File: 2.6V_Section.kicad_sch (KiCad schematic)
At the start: 1 part, among them U3_6 TPS259620DDAR

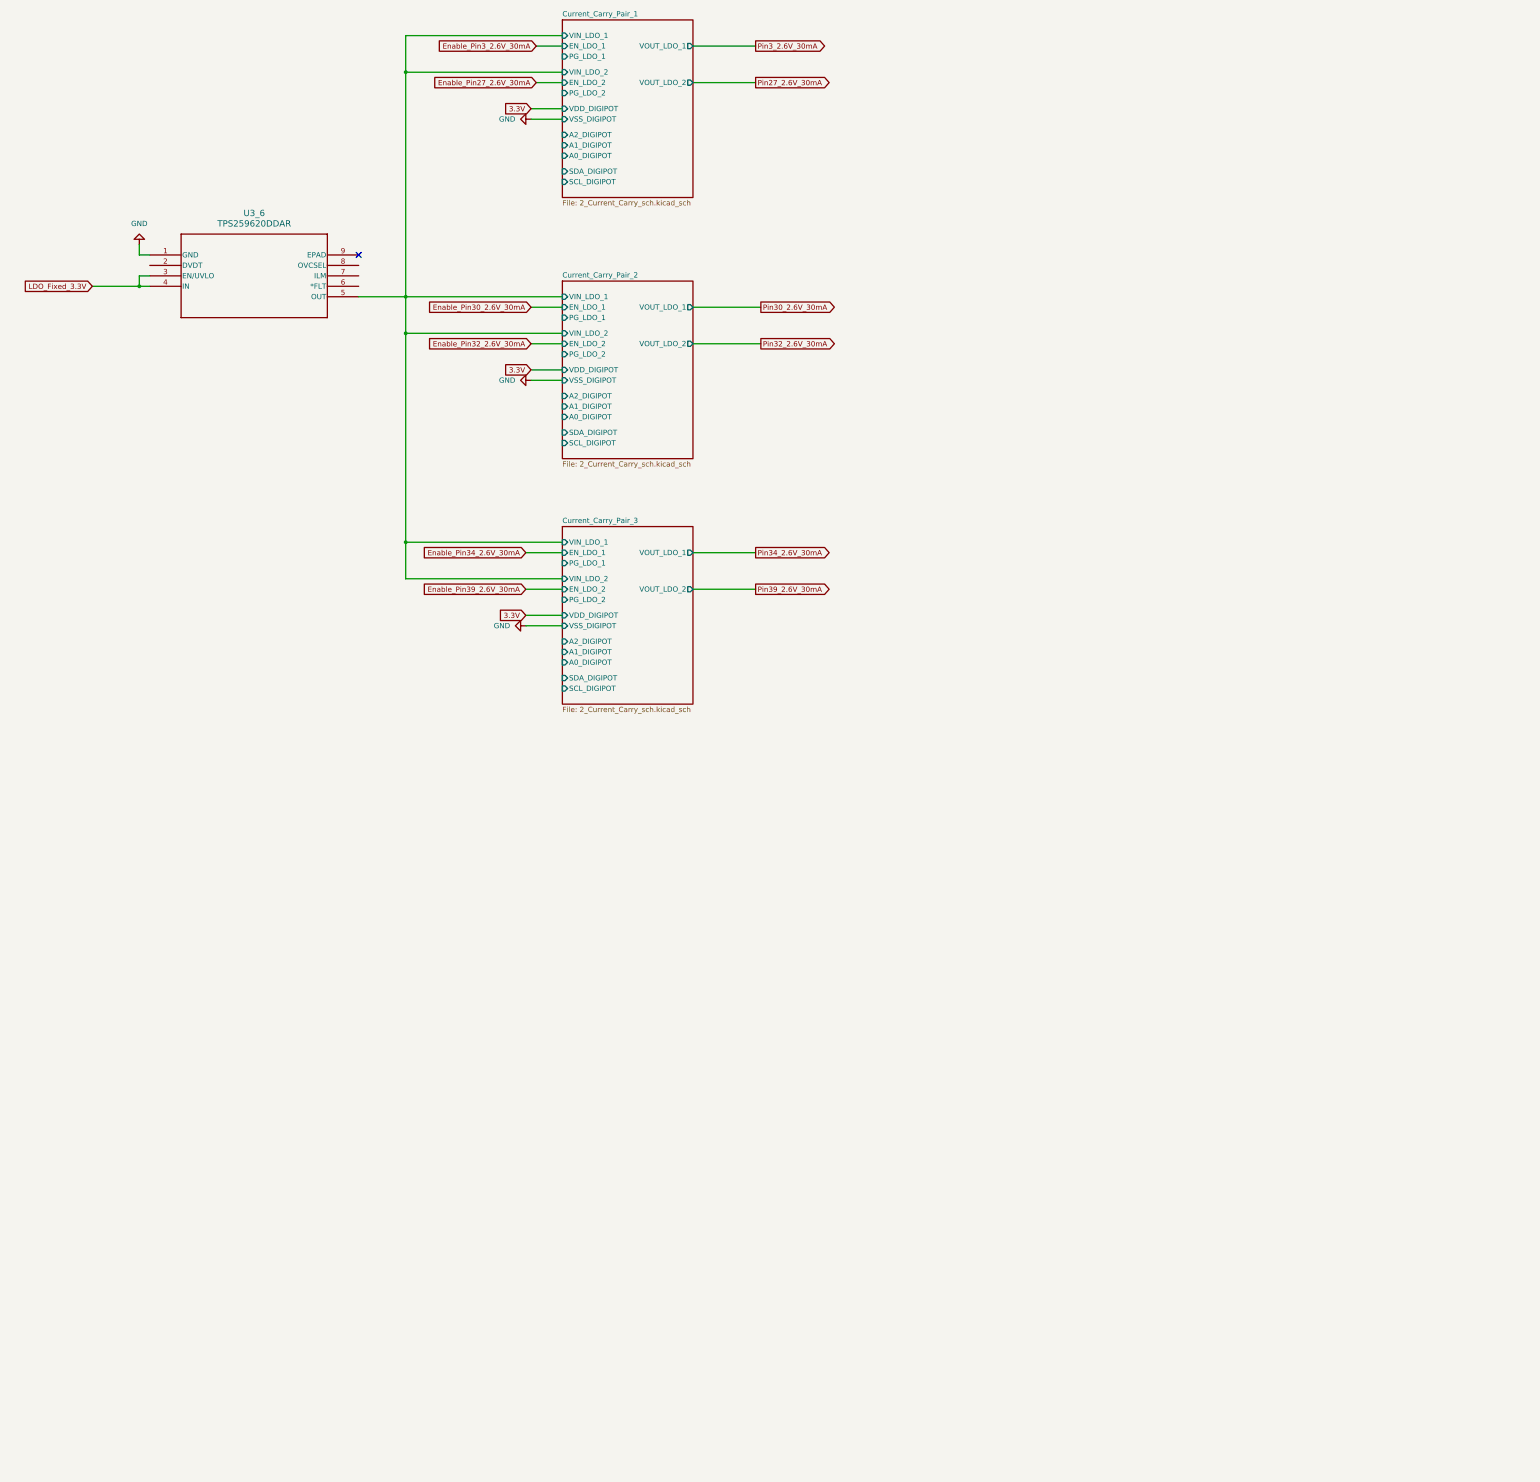
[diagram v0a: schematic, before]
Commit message: Full schematic connection without ratio consideration.
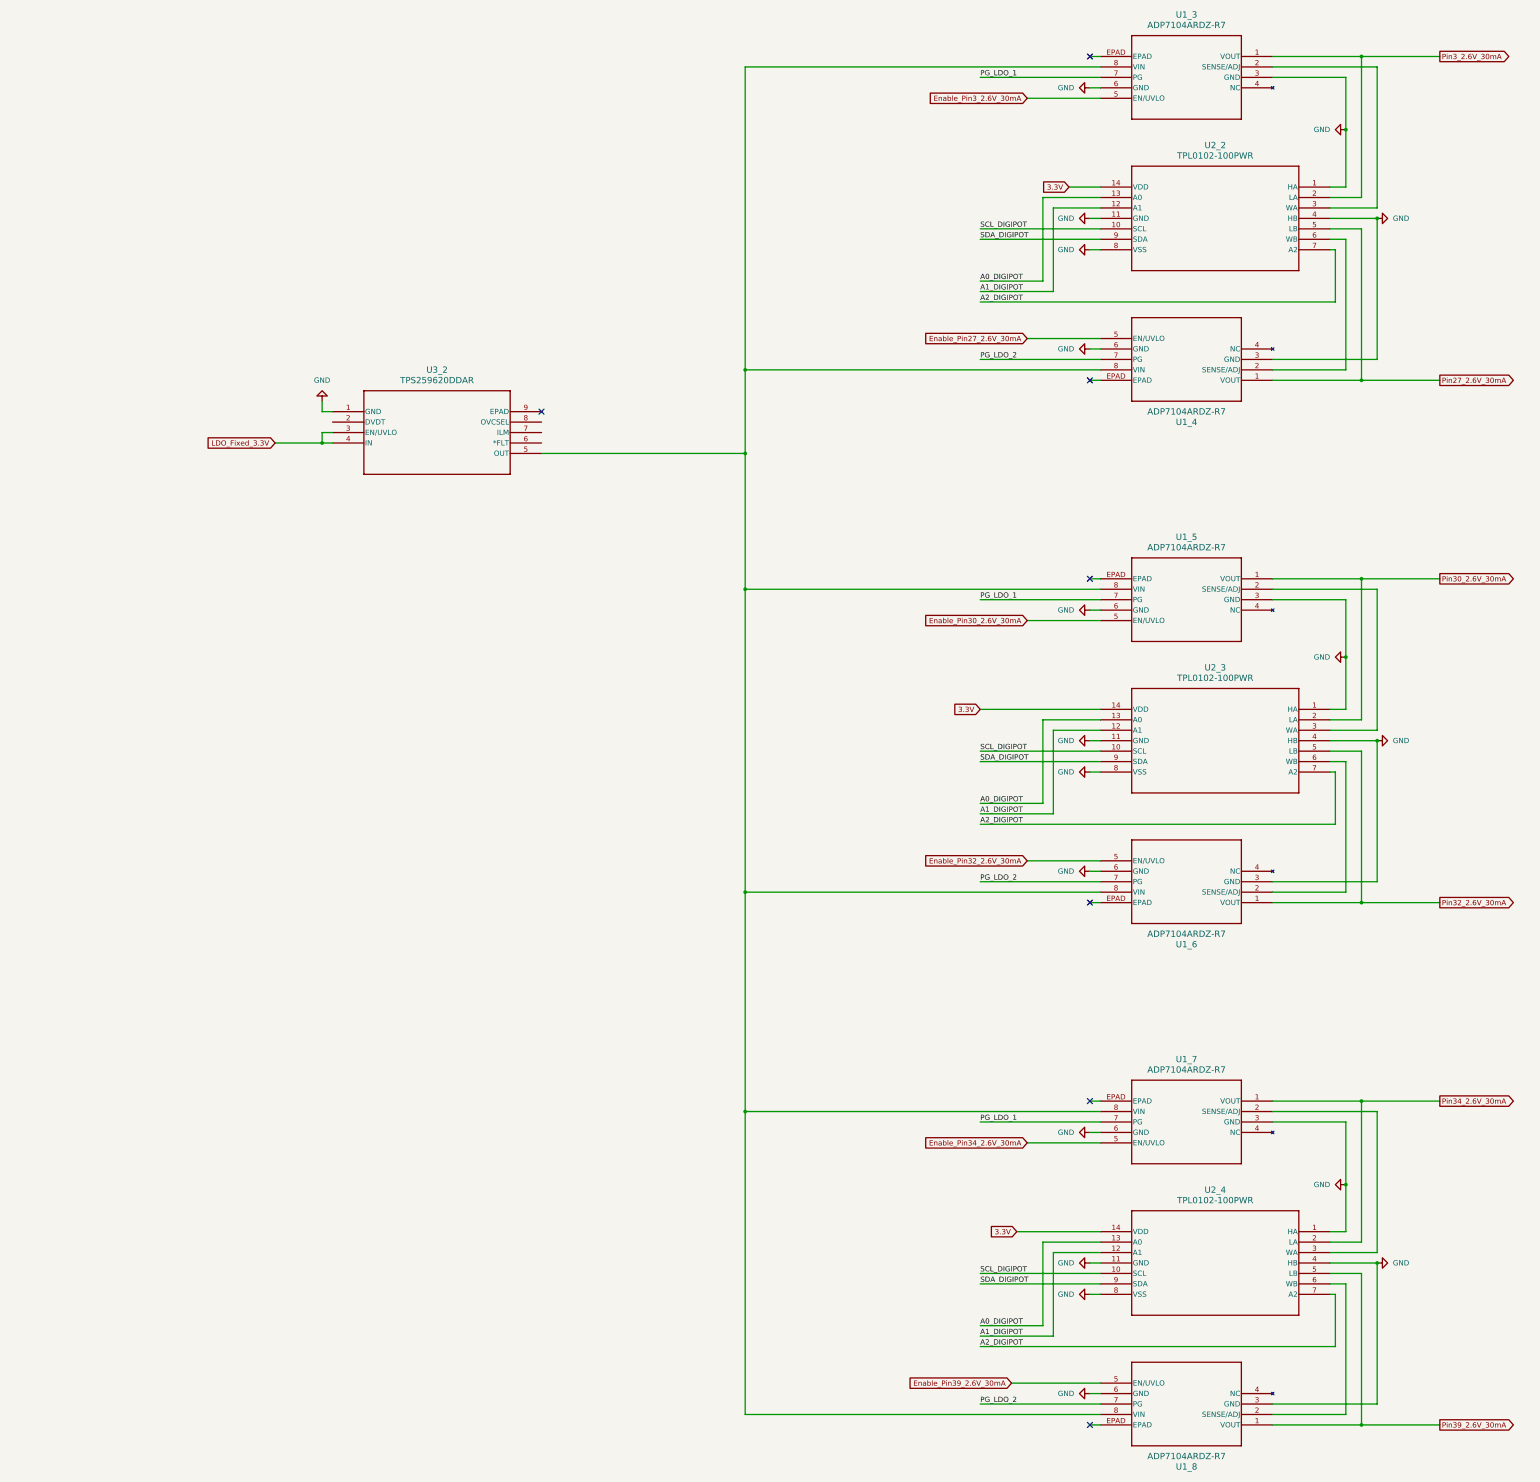
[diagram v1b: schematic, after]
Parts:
- added U1_3, U1_4, U1_5, U1_6, U1_7, U1_8: ADP7104ARDZ-R7, RD_8_2_ADI, symbol Adjustable Low-Dropout Regulator:ADP7104ARDZ-R7
- added U2_2, U2_3, U2_4: TPL0102-100PWR, PW14, symbol Digital Potentiometer:TPL0102-100PWR
- renumbered U3_6 to U3_2
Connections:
- net 3.3V: now also U2_2.14 (VDD), U2_3.14 (VDD), U2_4.14 (VDD)
- net Enable_Pin27_2.6V_30mA: now also U1_4.5 (EN/UVLO)
- net Enable_Pin30_2.6V_30mA: now also U1_5.5 (EN/UVLO)
- net Enable_Pin32_2.6V_30mA: now also U1_6.5 (EN/UVLO)
- net Enable_Pin34_2.6V_30mA: now also U1_7.5 (EN/UVLO)
- net Enable_Pin39_2.6V_30mA: now also U1_8.5 (EN/UVLO)
- net Enable_Pin3_2.6V_30mA: now also U1_3.5 (EN/UVLO)
- net GND: now also U1_3.3 (GND), U1_3.6 (GND), U1_4.3 (GND), U1_4.6 (GND), U1_5.3 (GND), U1_5.6 (GND), U1_6.3 (GND), U1_6.6 (GND), U1_7.3 (GND), U1_7.6 (GND), U1_8.3 (GND), U1_8.6 (GND), U2_2.1 (HA), U2_2.11 (GND), U2_2.4 (HB), U2_2.8 (VSS), U2_3.1 (HA), U2_3.11 (GND), U2_3.4 (HB), U2_3.8 (VSS), U2_4.1 (HA), U2_4.11 (GND), U2_4.4 (HB), U2_4.8 (VSS)
- net Pin27_2.6V_30mA: now also U1_4.1 (VOUT), U2_2.5 (LB)
- net Pin30_2.6V_30mA: now also U1_5.1 (VOUT), U2_3.2 (LA)
- net Pin32_2.6V_30mA: now also U1_6.1 (VOUT), U2_3.5 (LB)
- net Pin34_2.6V_30mA: now also U1_7.1 (VOUT), U2_4.2 (LA)
- net Pin39_2.6V_30mA: now also U1_8.1 (VOUT), U2_4.5 (LB)
- net Pin3_2.6V_30mA: now also U1_3.1 (VOUT), U2_2.2 (LA)
- net Current_Carry_Pair_1/VIN_LDO_1: no longer names the net of U3_2.5 (OUT)
- net Current_Carry_Pair_1/VIN_LDO_1: now also U1_3.8 (VIN), U1_4.8 (VIN), U1_5.8 (VIN), U1_6.8 (VIN), U1_7.8 (VIN), U1_8.8 (VIN)
- new net: U1_7.2 (SENSE/ADJ), U2_4.3 (WA)
- new net: U1_3.2 (SENSE/ADJ), U2_2.3 (WA)
- new net: U1_6.2 (SENSE/ADJ), U2_3.6 (WB)
- new net: U1_8.2 (SENSE/ADJ), U2_4.6 (WB)
- new net: U1_4.2 (SENSE/ADJ), U2_2.6 (WB)
- new net: U1_5.2 (SENSE/ADJ), U2_3.3 (WA)
- new net A0_DIGIPOT: U2_2.13 (A0), U2_3.13 (A0), U2_4.13 (A0)
- new net A1_DIGIPOT: U2_2.12 (A1), U2_3.12 (A1), U2_4.12 (A1)
- new net A2_DIGIPOT: U2_2.7 (A2), U2_3.7 (A2), U2_4.7 (A2)
- new net PG_LDO_1: U1_3.7 (PG), U1_5.7 (PG), U1_7.7 (PG)
- new net PG_LDO_2: U1_4.7 (PG), U1_6.7 (PG), U1_8.7 (PG)
- new net SCL_DIGIPOT: U2_2.10 (SCL), U2_3.10 (SCL), U2_4.10 (SCL)
- new net SDA_DIGIPOT: U2_2.9 (SDA), U2_3.9 (SDA), U2_4.9 (SDA)
- no-connect marks 1 -> 7
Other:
- removed sheet Current_Carry_Pair_1
- removed sheet Current_Carry_Pair_2
- removed sheet Current_Carry_Pair_3
- moved on the sheet: U3_2
